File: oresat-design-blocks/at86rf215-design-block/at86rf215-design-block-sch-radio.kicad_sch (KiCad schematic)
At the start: 39 parts, among them J1 SMA, J2 USB4105-GF-A, J3 Conn_01x04, J5 Conn_02x20_Odd_Even, J6 Conn_01x04, SW1 RESET, U1 AT86RF215, U2 LP2985AIM5-1.8_NOPB, X1 TXETALSANF-26.000000

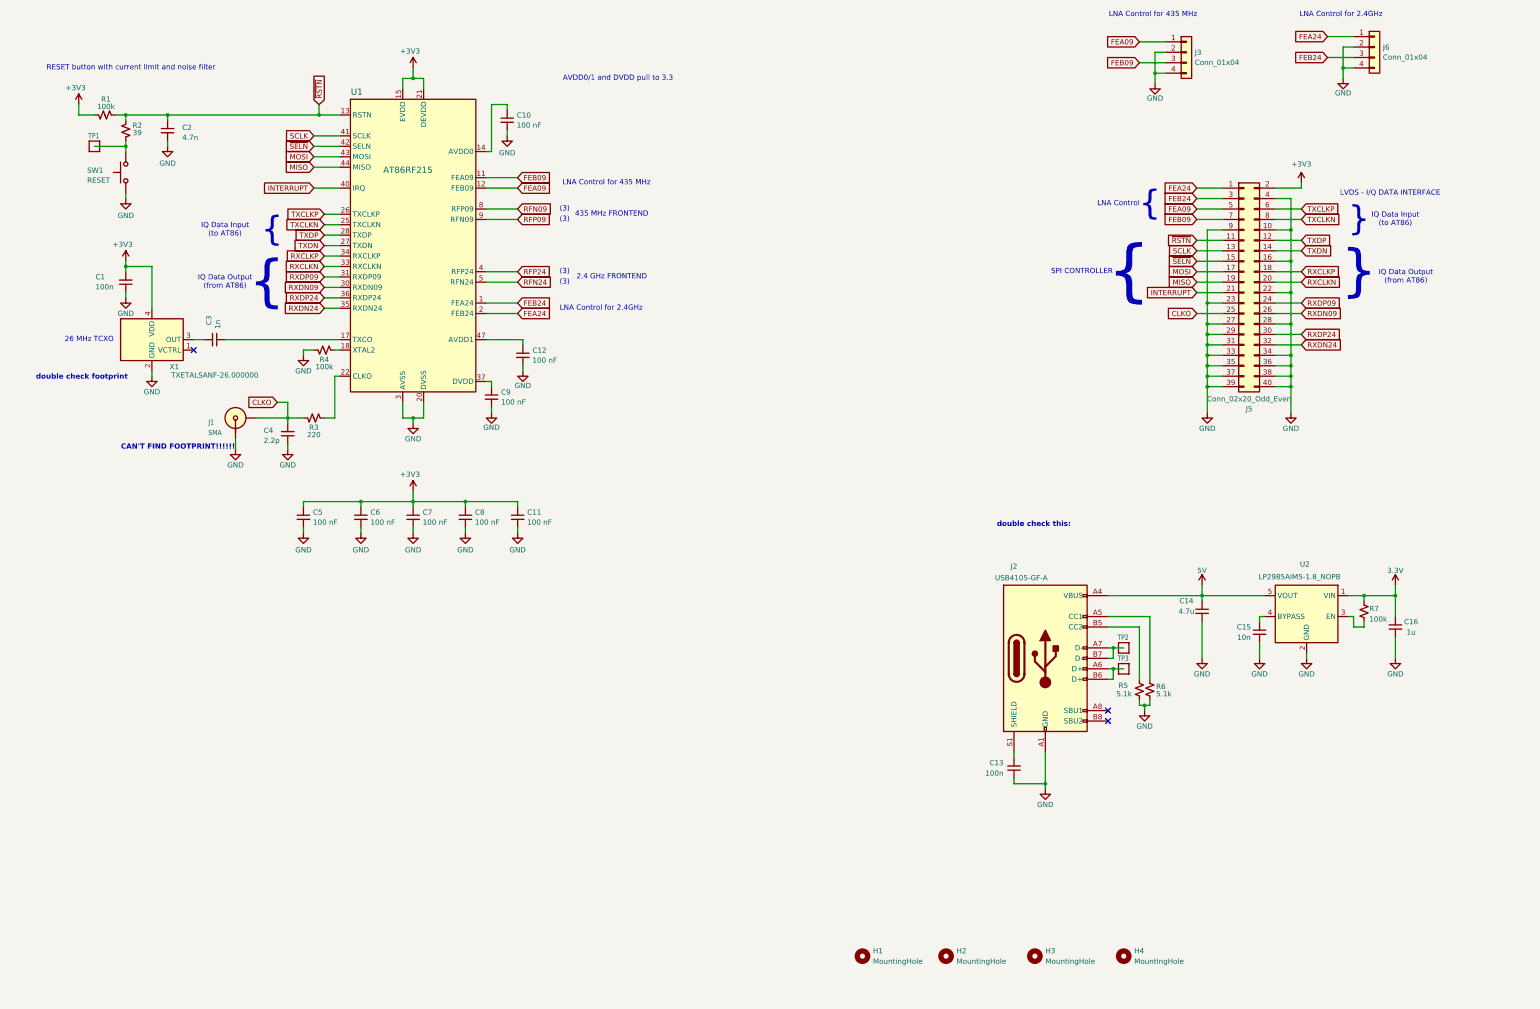
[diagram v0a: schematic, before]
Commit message: Design review and cleanup of AT86RF215 eval board; ready for layout.
Added footprints to SMAs, made a symbol for a balun, cleaned up and renamed schematic. Added terminal block for power just cause.
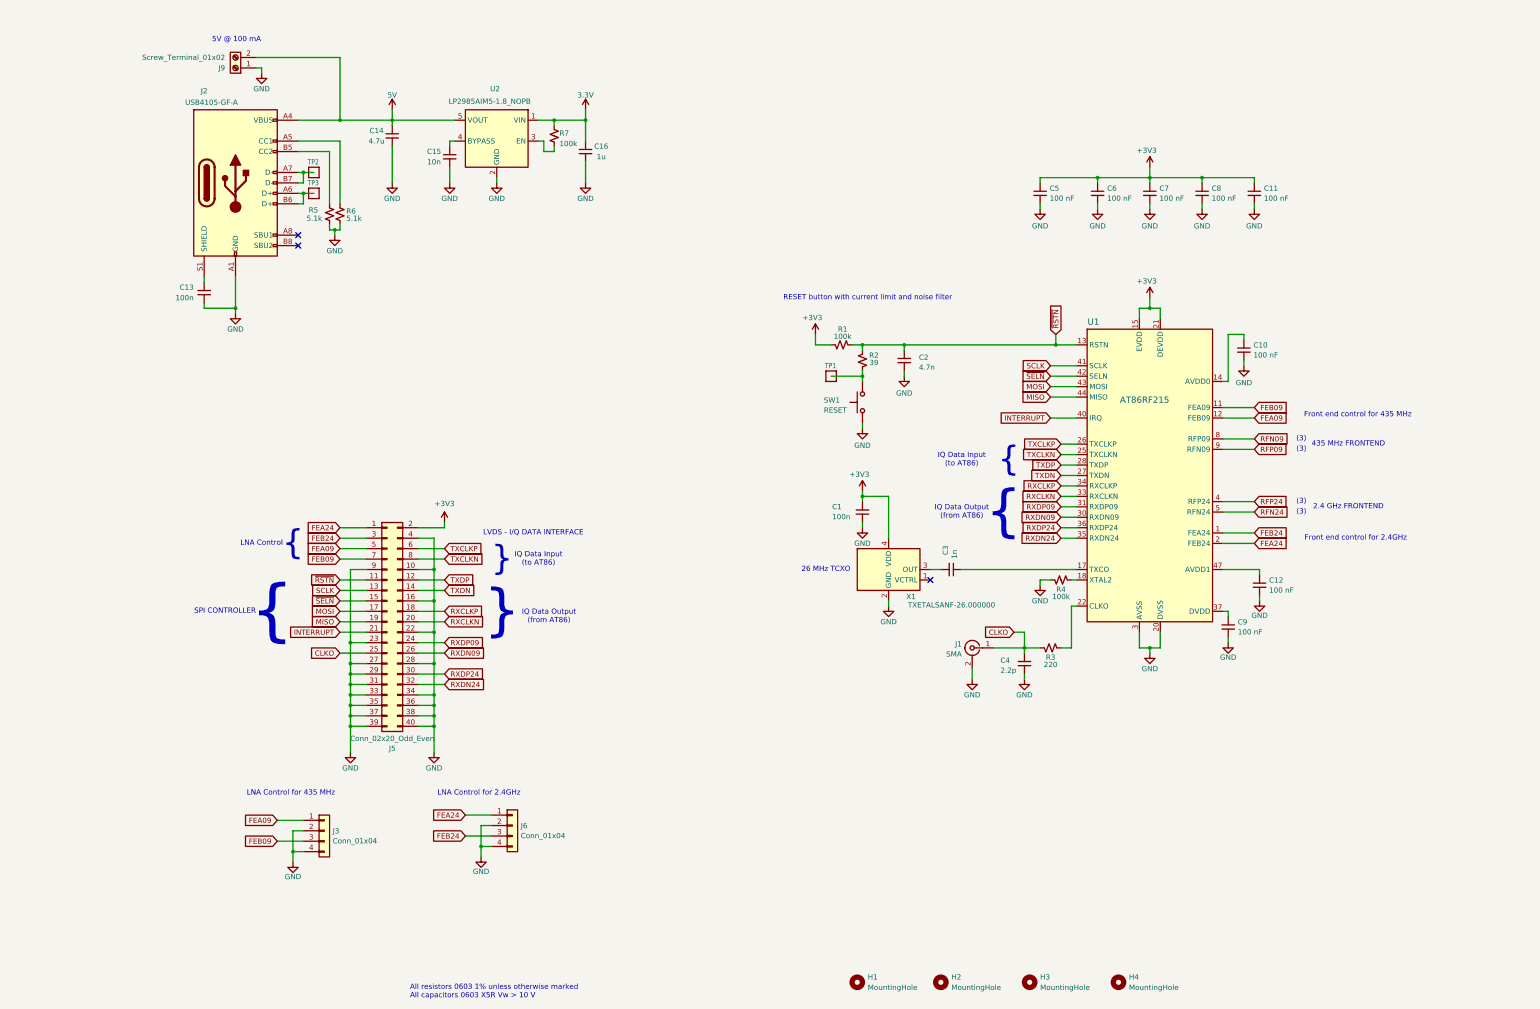
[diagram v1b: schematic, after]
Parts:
- removed J1: SMA, Connector_Coaxial:SMA_Samtec_SMA-J-P-H-ST-EM1_EdgeMount, symbol oresat-connectors:J-MOLEX-SMPM-73300-002X
- added J1: SMA, Connector_Coaxial:SMA_Samtec_SMA-J-P-H-ST-EM1_EdgeMount, symbol Connector:Conn_Coaxial
- added J9: Screw_Terminal_01x02, TerminalBlock_Phoenix:TerminalBlock_Phoenix_PT-1,5-2-3.5-H_1x02_P3.50mm_Horizontal, symbol Connector:Screw_Terminal_01x02
- C14, C15, C16: DIS (none) -> DigiKey; DST Digi-Key -> (none)
- J3, J6: footprint (none) -> Connector_PinHeader_2.54mm:PinHeader_1x04_P2.54mm_Vertical
- R1, R4: DIS (none) -> Digikey; DPN (none) -> RMCF0603FT100KCT-ND; MFR (none) -> Stackpole Electronics Inc; MPN (none) -> RMCF0603FT100K
- R7: DIS (none) -> Digikey; DST Digi-Key -> (none)
- U2: DST Digi-Key -> (none)
- X1: DIS (none) -> DigiKey; DPN (none) -> 1664-TXETALSANF-26.000000CT-ND; MFR (none) -> Taitien; MPN (none) -> TXETALSANF-26.000000
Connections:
- net 5V: now also J9.2 (Pin_2)
- net AVSS: now also J1.2 (Ext), J9.1 (Pin_1)
- net CLKO: now also J1.1 (In)
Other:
- note added: "5V @ 100 mA"
- note added: "All resistors 0603 1% unless otherwise marked All capacitors 0603 X5R Vw > 10 V"
- note added: "Front end control for 2.4GHz"
- note added: "Front end control for 435 MHz"
- note removed: "AVDD0/1 and DVDD pull to 3.3"
- note removed: "CAN'T FIND FOOTPRINT!!!!!!"
- note removed: "double check footprint"
- note removed: "double check this:"
- moved on the sheet: C1, C10, C11, C12, C13, C14, C15, C16, C2, C3, C4, C5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

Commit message: started component layout and initial routing on PCB
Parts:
- C3: footprint Capacitor_SMD:C_0603_1608Metric -> Capacitor_SMD:C_0402_1005Metric
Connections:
- net 3.3V is gone; now on net +3.3V: C16.1, R7.1, U2.1 (VIN)
- net AVSS: now also J5.21 (Pin_21), J5.25 (Pin_25), J5.3 (Pin_3), J5.7 (Pin_7); no longer J5.10 (Pin_10), J5.16 (Pin_16), J5.22 (Pin_22), J5.23 (Pin_23), J5.28 (Pin_28), J5.34 (Pin_34), J5.36 (Pin_36), J5.37 (Pin_37), J5.4 (Pin_4), J5.9 (Pin_9)
- net CLKO: now also J5.23 (Pin_23); no longer J5.25 (Pin_25)
- net FEA09: now also J5.2 (Pin_2); no longer J5.5 (Pin_5)
- net FEB09: now also J5.6 (Pin_6); no longer J5.7 (Pin_7)
- net FEB24: now also J5.5 (Pin_5); no longer J5.3 (Pin_3)
- net INTERRUPT: now also J5.19 (Pin_19); no longer J5.21 (Pin_21)
- net MISO: now also J5.17 (Pin_17); no longer J5.19 (Pin_19)
- net MOSI: now also J5.15 (Pin_15); no longer J5.17 (Pin_17)
- net RXCLKN: now also J5.24 (Pin_24); no longer J5.20 (Pin_20)
- net RXCLKP: now also J5.22 (Pin_22); no longer J5.18 (Pin_18)
- net RXDN09: now also J5.30 (Pin_30); no longer J5.26 (Pin_26)
- net RXDN24: now also J5.36 (Pin_36); no longer J5.32 (Pin_32)
- net RXDP09: now also J5.28 (Pin_28); no longer J5.24 (Pin_24)
- net RXDP24: now also J5.34 (Pin_34); no longer J5.30 (Pin_30)
- net SCLK: now also J5.11 (Pin_11); no longer J5.13 (Pin_13)
- net TXCLKN: now also J5.12 (Pin_12); no longer J5.8 (Pin_8)
- net TXCLKP: now also J5.10 (Pin_10); no longer J5.6 (Pin_6)
- net TXDN: now also J5.18 (Pin_18); no longer J5.14 (Pin_14)
- net TXDP: now also J5.16 (Pin_16); no longer J5.12 (Pin_12)
- net ~{RSTN}: now also J5.9 (Pin_9); no longer J5.11 (Pin_11)
- net ~{SELN}: now also J5.13 (Pin_13); no longer J5.15 (Pin_15)
- net +3V3 renamed +3.3V
- net +3.3V: now also J5.37 (Pin_37); no longer J5.2 (Pin_2)
- net 5V renamed +5V
- new net: J5.14 (Pin_14), J5.20 (Pin_20), J5.26 (Pin_26), J5.32 (Pin_32), J5.4 (Pin_4), J5.8 (Pin_8)
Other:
- note added: "Front end control"
- note added: "breakup 20 pin connector"
- note removed: "LNA Control"
- note removed: "LNA Control for 2.4GHz"
- note removed: "LNA Control for 435 MHz"

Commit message: more routing progress
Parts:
- added J10: Conn_01x07, Connector_PinHeader_2.54mm:PinHeader_1x04_P2.54mm_Vertical, symbol Connector_Generic:Conn_01x07
- added J11: Conn_01x05, Connector_PinHeader_2.54mm:PinHeader_1x04_P2.54mm_Vertical, symbol Connector_Generic:Conn_01x05
- added J12: Conn_01x08, Connector_PinHeader_2.54mm:PinHeader_1x04_P2.54mm_Vertical, symbol Connector_Generic:Conn_01x08
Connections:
- net AVSS: now also J11.3 (Pin_3), J12.3 (Pin_3), J12.6 (Pin_6)
- net CLKO: now also J10.1 (Pin_1)
- net INTERRUPT: now also J10.7 (Pin_7)
- net MISO: now also J10.6 (Pin_6)
- net MOSI: now also J10.5 (Pin_5)
- net RXCLKN: now also J12.7 (Pin_7)
- net RXCLKP: now also J12.8 (Pin_8)
- net RXDN09: now also J12.4 (Pin_4)
- net RXDN24: now also J12.1 (Pin_1)
- net RXDP09: now also J12.5 (Pin_5)
- net RXDP24: now also J12.2 (Pin_2)
- net SCLK: now also J10.3 (Pin_3)
- net TXCLKN: now also J11.4 (Pin_4)
- net TXCLKP: now also J11.5 (Pin_5)
- net TXDN: now also J11.1 (Pin_1)
- net TXDP: now also J11.2 (Pin_2)
- net ~{RSTN}: now also J10.2 (Pin_2)
- net ~{SELN}: now also J10.4 (Pin_4)
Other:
- note removed: "breakup 20 pin connector"
- moved on the sheet: J3, J5, J6

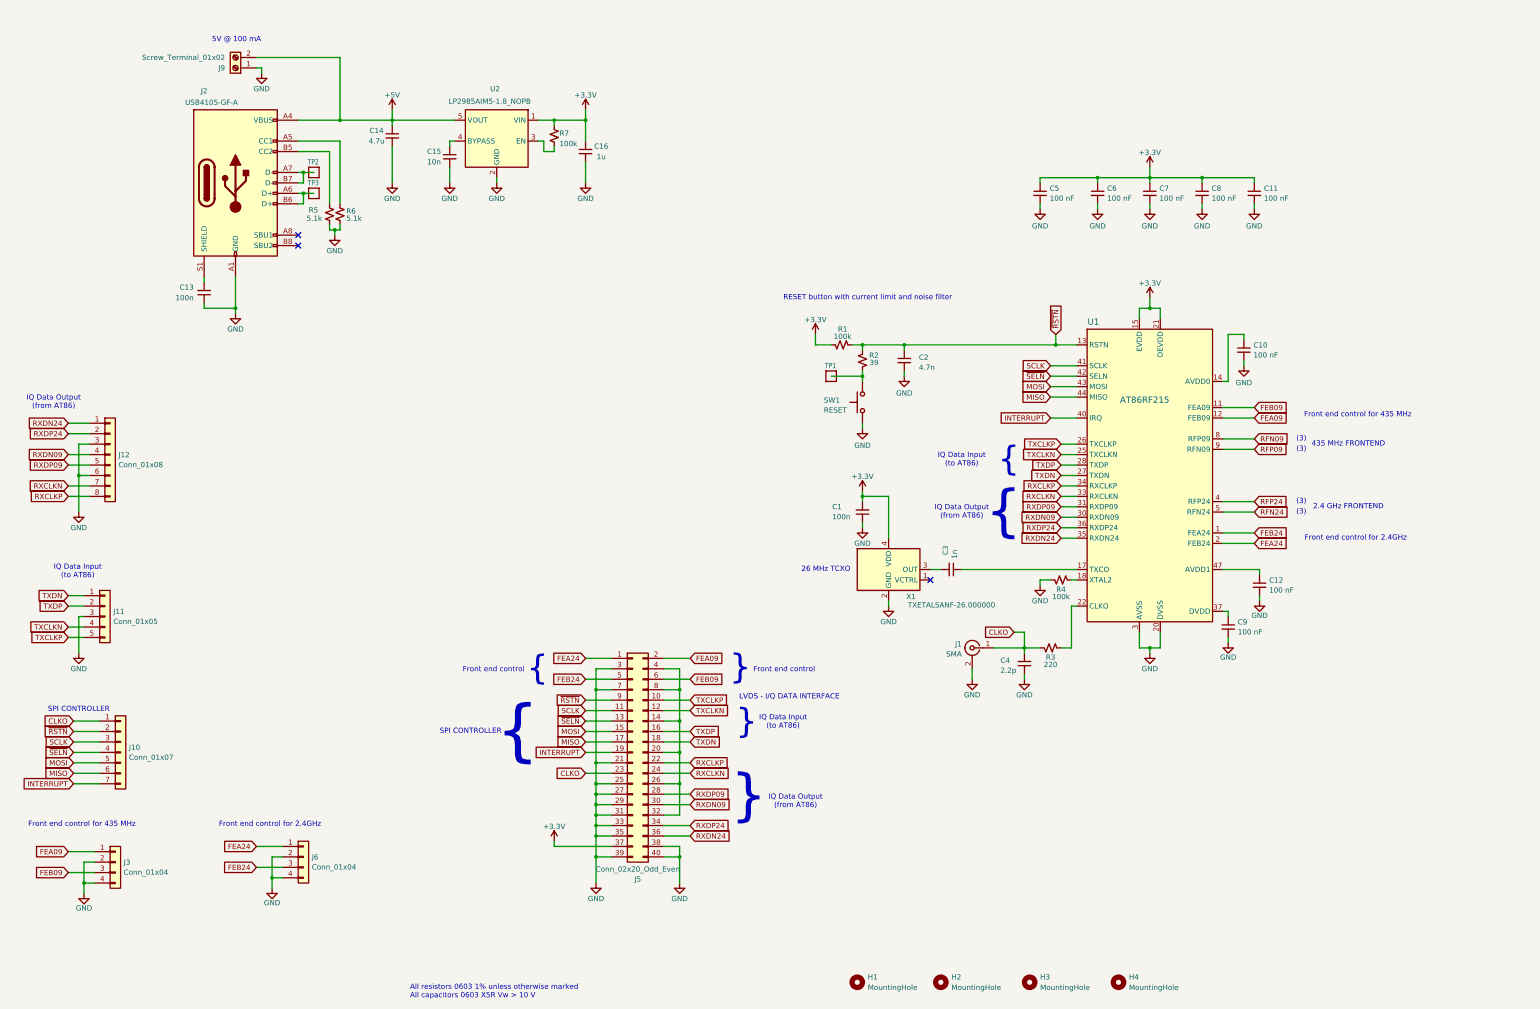
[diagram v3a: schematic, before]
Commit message: completed initial routing, changed pin out and added voltage divider to QPC1022 CTRL pin
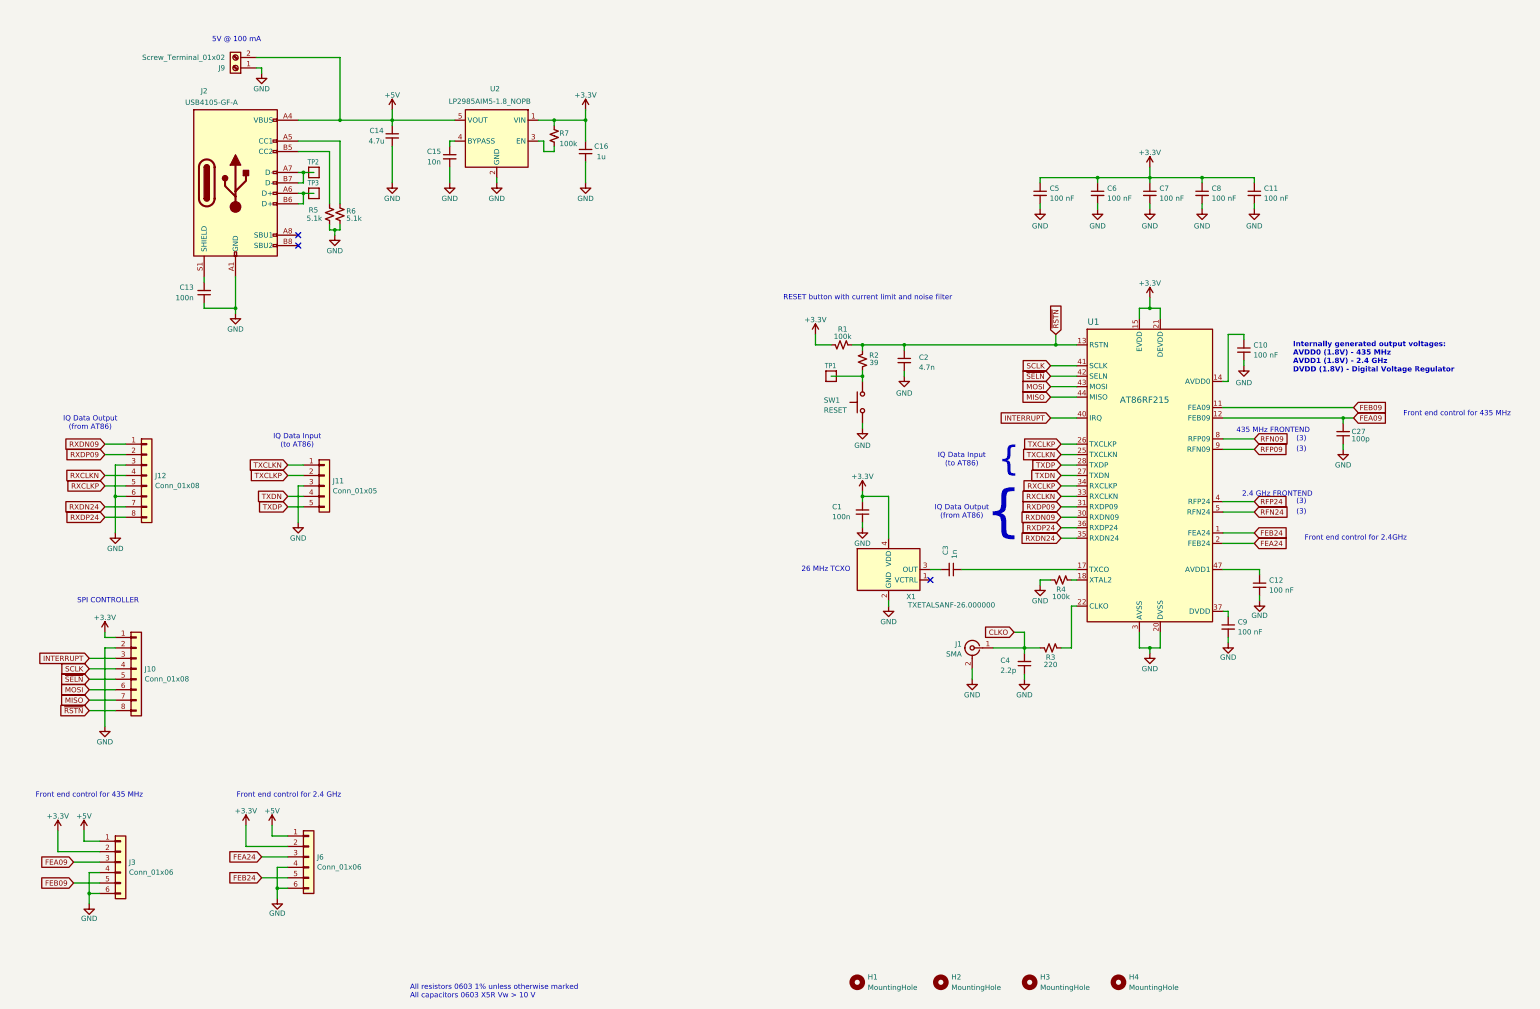
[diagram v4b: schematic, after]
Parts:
- removed J5: Conn_02x20_Odd_Even, Connector_PinHeader_2.54mm:PinHeader_2x20_P2.54mm_Vertical, symbol Connector_Generic:Conn_02x20_Odd_Even
- added C27: 100p, oresat-passives:0402-C, symbol Device:C_Small
- J10: value Conn_01x07 -> Conn_01x08; footprint Connector_PinHeader_2.54mm:PinHeader_1x04_P2.54mm_Vertical -> Connector_PinHeader_2.54mm:PinHeader_1x08_P2.54mm_Vertical; symbol Connector_Generic:Conn_01x07 -> Connector_Generic:Conn_01x08
- J11: footprint Connector_PinHeader_2.54mm:PinHeader_1x04_P2.54mm_Vertical -> Connector_PinHeader_2.54mm:PinHeader_1x05_P2.54mm_Vertical
- J12: footprint Connector_PinHeader_2.54mm:PinHeader_1x04_P2.54mm_Vertical -> Connector_PinHeader_2.54mm:PinHeader_1x08_P2.54mm_Vertical
- J3, J6: value Conn_01x04 -> Conn_01x06; footprint Connector_PinHeader_2.54mm:PinHeader_1x04_P2.54mm_Vertical -> Connector_PinHeader_2.54mm:PinHeader_1x06_P2.54mm_Vertical; symbol Connector_Generic:Conn_01x04 -> Connector_Generic:Conn_01x06
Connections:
- net +3.3V: now also J10.1 (Pin_1), J3.2 (Pin_2), J6.2 (Pin_2)
- net +5V: now also J3.1 (Pin_1), J6.1 (Pin_1)
- net AVSS: now also J10.2 (Pin_2), J3.6 (Pin_6), J6.6 (Pin_6), C27.1; no longer J3.2 (Pin_2), J6.2 (Pin_2)
- net CLKO: no longer J10.1 (Pin_1)
- net FEA09: now also J3.3 (Pin_3), C27.2; no longer J3.1 (Pin_1)
- net FEA24: now also J6.3 (Pin_3); no longer J6.1 (Pin_1)
- net FEB09: now also J3.5 (Pin_5); no longer J3.3 (Pin_3)
- net FEB24: now also J6.5 (Pin_5); no longer J6.3 (Pin_3)
- net INTERRUPT: now also J10.3 (Pin_3); no longer J10.7 (Pin_7)
- net MISO: now also J10.7 (Pin_7); no longer J10.6 (Pin_6)
- net MOSI: now also J10.6 (Pin_6); no longer J10.5 (Pin_5)
- net RXCLKN: now also J12.4 (Pin_4); no longer J12.7 (Pin_7)
- net RXCLKP: now also J12.5 (Pin_5); no longer J12.8 (Pin_8)
- net RXDN09: now also J12.1 (Pin_1); no longer J12.4 (Pin_4)
- net RXDN24: now also J12.7 (Pin_7); no longer J12.1 (Pin_1)
- net RXDP09: now also J12.2 (Pin_2); no longer J12.5 (Pin_5)
- net RXDP24: now also J12.8 (Pin_8); no longer J12.2 (Pin_2)
- net SCLK: now also J10.4 (Pin_4); no longer J10.3 (Pin_3)
- net TXCLKN: now also J11.1 (Pin_1); no longer J11.4 (Pin_4)
- net TXCLKP: now also J11.2 (Pin_2); no longer J11.5 (Pin_5)
- net TXDN: now also J11.4 (Pin_4); no longer J11.1 (Pin_1)
- net TXDP: now also J11.5 (Pin_5); no longer J11.2 (Pin_2)
- net ~{RSTN}: now also J10.8 (Pin_8); no longer J10.2 (Pin_2)
- net ~{SELN}: now also J10.5 (Pin_5); no longer J10.4 (Pin_4)
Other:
- note added: "Front end control for 2.4 GHz"
- note added: "Internally generated output voltages: AVDD0 (1.8V) - 435 MHz AVDD1 (1.8V) - 2.4 GHz DVDD (1.8V) - Digital Voltage Regulator"
- note removed: "Front end control"
- note removed: "LVDS - I/Q DATA INTERFACE"
- note removed: "}"
- moved on the sheet: J11, J12
